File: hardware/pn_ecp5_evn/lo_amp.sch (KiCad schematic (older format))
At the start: 22 parts, among them J401 Conn_Coaxial, U301 PAT1220-C-3DB, U302 TRF37A73, U303 PAT1220-C-3DB

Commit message: first pass footprint assignment on pn r0
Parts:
- C301, C302, C303, C304, C305, C307, C308: footprint (none) -> Capacitor_SMD:C_0402_1005Metric
- C306, C309: footprint (none) -> Capacitor_SMD:C_0603_1608Metric
- J401: footprint (none) -> Connector_Coaxial:U.FL_Hirose_U.FL-R-SMT-1_Vertical
- L301, L302, L303: footprint (none) -> Inductor_SMD:L_0402_1005Metric
- R301, R302, R303, R304, R305, R306: footprint (none) -> Resistor_SMD:R_0402_1005Metric
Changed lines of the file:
@@
 $Descr A4 11693 8268
 encoding utf-8
-Sheet 3 9
+Sheet 4 9
 Title ""
 Date ""
@@
 F 0 "R401" H 3659 4396 50  0000 L CNN
 F 1 "50" H 3659 4305 50  0000 L CNN
-F 2 "" H 3600 4350 50  0001 C CNN
+F 2 "Resistor_SMD:R_0402_1005Metric" H 3600 4350 50  0001 C CNN
 F 3 "~" H 3600 4350 50  0001 C CNN
 	1    3600 4350
@@
 F 0 "C402" V 3950 4100 50  0000 C CNN
 F 1 "10 nF" V 3950 4350 50  0000 C CNN
-F 2 "" H 4000 4200 50  0001 C CNN
+F 2 "Capacitor_SMD:C_0402_1005Metric" H 4000 4200 50  0001 C CNN
 F 3 "~" H 4000 4200 50  0001 C CNN
 	1    4000 4200
@@
 F 0 "C403" V 3950 4800 50  0000 C CNN
 F 1 "10 nF" V 3950 5050 50  0000 C CNN
-F 2 "" H 4000 4900 50  0001 C CNN
+F 2 "Capacitor_SMD:C_0402_1005Metric" H 4000 4900 50  0001 C CNN
 F 3 "~" H 4000 4900 50  0001 C CNN
 	1    4000 4900
@@
 F 0 "R402" H 3659 4796 50  0000 L CNN
 F 1 "50" H 3659 4705 50  0000 L CNN
-F 2 "" H 3600 4750 50  0001 C CNN
+F 2 "Resistor_SMD:R_0402_1005Metric" H 3600 4750 50  0001 C CNN
 F 3 "~" H 3600 4750 50  0001 C CNN
 	1    3600 4750
@@
 F 0 "C401" V 3300 4500 50  0000 C CNN
 F 1 "10 nF" V 3500 4600 50  0000 C CNN
-F 2 "" H 3400 4550 50  0001 C CNN
+F 2 "Capacitor_SMD:C_0402_1005Metric" H 3400 4550 50  0001 C CNN
 F 3 "~" H 3400 4550 50  0001 C CNN
 	1    3400 4550
@@
 F 0 "L401" V 3950 4550 50  0000 C CNN
 F 1 "18 nH" V 3800 4500 50  0000 C CNN
-F 2 "" H 3850 4550 50  0001 C CNN
+F 2 "Inductor_SMD:L_0402_1005Metric" H 3850 4550 50  0001 C CNN
 F 3 "~" H 3850 4550 50  0001 C CNN
 	1    3850 4550
@@
 F 0 "R404" H 4459 4946 50  0000 L CNN
 F 1 "50" H 4459 4855 50  0000 L CNN
-F 2 "" H 4400 4900 50  0001 C CNN
+F 2 "Resistor_SMD:R_0402_1005Metric" H 4400 4900 50  0001 C CNN
 F 3 "~" H 4400 4900 50  0001 C CNN
 	1    4400 4900
@@
 F 0 "C404" V 5321 4200 50  0000 C CNN
 F 1 "10 nF" V 5412 4200 50  0000 C CNN
-F 2 "" H 5550 4200 50  0001 C CNN
+F 2 "Capacitor_SMD:C_0402_1005Metric" H 5550 4200 50  0001 C CNN
 F 3 "~" H 5550 4200 50  0001 C CNN
 	1    5550 4200
@@
 F 0 "C407" V 6571 4200 50  0000 C CNN
 F 1 "10 nF" V 6662 4200 50  0000 C CNN
-F 2 "" H 6800 4200 50  0001 C CNN
+F 2 "Capacitor_SMD:C_0402_1005Metric" H 6800 4200 50  0001 C CNN
 F 3 "~" H 6800 4200 50  0001 C CNN
 	1    6800 4200
@@
 F 0 "L403" H 6498 3646 50  0000 L CNN
 F 1 "BLM15GG471" H 6498 3555 50  0000 L CNN
-F 2 "" H 6450 3600 50  0001 C CNN
+F 2 "Inductor_SMD:L_0402_1005Metric" H 6450 3600 50  0001 C CNN
 F 3 "~" H 6450 3600 50  0001 C CNN
 	1    6450 3600
@@
 F 0 "C405" H 5742 3146 50  0000 L CNN
 F 1 "100 nF" H 5742 3055 50  0000 L CNN
-F 2 "" H 5650 3100 50  0001 C CNN
+F 2 "Capacitor_SMD:C_0402_1005Metric" H 5650 3100 50  0001 C CNN
 F 3 "~" H 5650 3100 50  0001 C CNN
 	1    5650 3100
@@
 F 0 "C409" H 7592 3146 50  0000 L CNN
 F 1 "10 uF" H 7592 3055 50  0000 L CNN
-F 2 "" H 7500 3100 50  0001 C CNN
+F 2 "Capacitor_SMD:C_0603_1608Metric" H 7500 3100 50  0001 C CNN
 F 3 "~" H 7500 3100 50  0001 C CNN
 	1    7500 3100
@@
 F 0 "C408" H 7192 3146 50  0000 L CNN
 F 1 "10 nF" H 7192 3055 50  0000 L CNN
-F 2 "" H 7100 3100 50  0001 C CNN
+F 2 "Capacitor_SMD:C_0402_1005Metric" H 7100 3100 50  0001 C CNN
 F 3 "~" H 7100 3100 50  0001 C CNN
 	1    7100 3100
@@
 F 0 "C406" H 6742 3146 50  0000 L CNN
 F 1 "390 pF" H 6742 3055 50  0000 L CNN
-F 2 "" H 6650 3100 50  0001 C CNN
+F 2 "Capacitor_SMD:C_0603_1608Metric" H 6650 3100 50  0001 C CNN
 F 3 "~" H 6650 3100 50  0001 C CNN
 	1    6650 3100
@@
 F 0 "J401" H 4900 5175 50  0000 L CNN
 F 1 "Conn_Coaxial" H 4900 5084 50  0000 L CNN
-F 2 "" H 4800 5200 50  0001 C CNN
+F 2 "Connector_Coaxial:U.FL_Hirose_U.FL-R-SMT-1_Vertical" H 4800 5200 50  0001 C CNN
 F 3 " ~" H 4800 5200 50  0001 C CNN
 	1    4800 5200
@@
 F 0 "R405" H 4459 5246 50  0000 L CNN
 F 1 "DNI" H 4459 5155 50  0000 L CNN
-F 2 "" H 4400 5200 50  0001 C CNN
+F 2 "Resistor_SMD:R_0402_1005Metric" H 4400 5200 50  0001 C CNN
 F 3 "~" H 4400 5200 50  0001 C CNN
 	1    4400 5200
@@
 F 0 "L402" H 6498 2446 50  0000 L CNN
 F 1 "BLM15GG471" H 6498 2355 50  0000 L CNN
-F 2 "" H 6450 2400 50  0001 C CNN
+F 2 "Inductor_SMD:L_0402_1005Metric" H 6450 2400 50  0001 C CNN
 F 3 "~" H 6450 2400 50  0001 C CNN
 	1    6450 2400
@@
 F 0 "R403" H 4459 3946 50  0000 L CNN
 F 1 "DNI" H 4459 3855 50  0000 L CNN
-F 2 "" H 4400 3900 50  0001 C CNN
+F 2 "Resistor_SMD:R_0402_1005Metric" H 4400 3900 50  0001 C CNN
 F 3 "~" H 4400 3900 50  0001 C CNN
 	1    4400 3900
@@
 F 0 "R406" H 6009 3746 50  0000 L CNN
 F 1 "DNI" H 6009 3655 50  0000 L CNN
-F 2 "" H 5950 3700 50  0001 C CNN
+F 2 "Resistor_SMD:R_0402_1005Metric" H 5950 3700 50  0001 C CNN
 F 3 "~" H 5950 3700 50  0001 C CNN
 	1    5950 3700

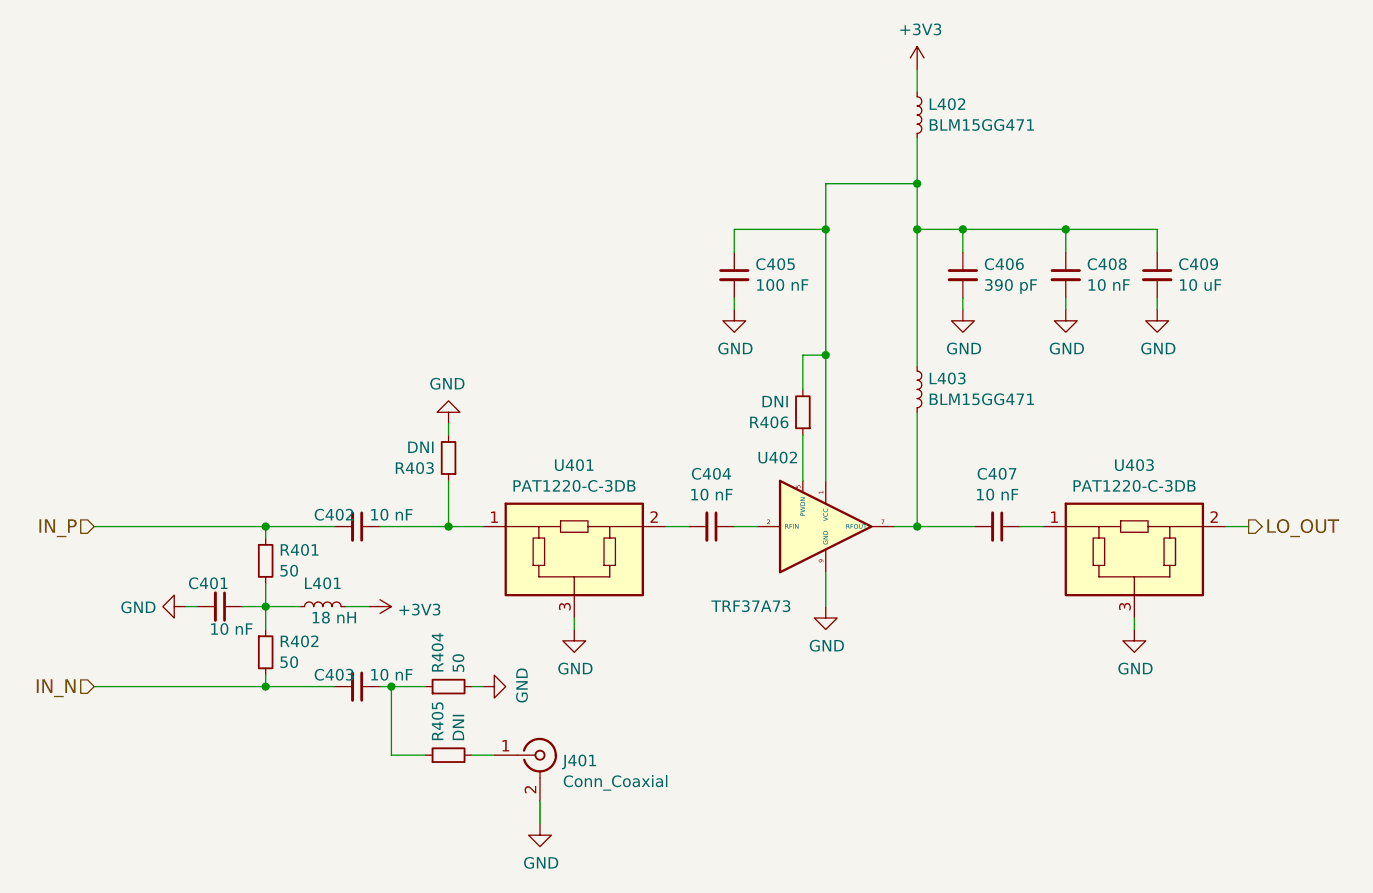
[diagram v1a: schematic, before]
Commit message: layout of phase noise downconverter
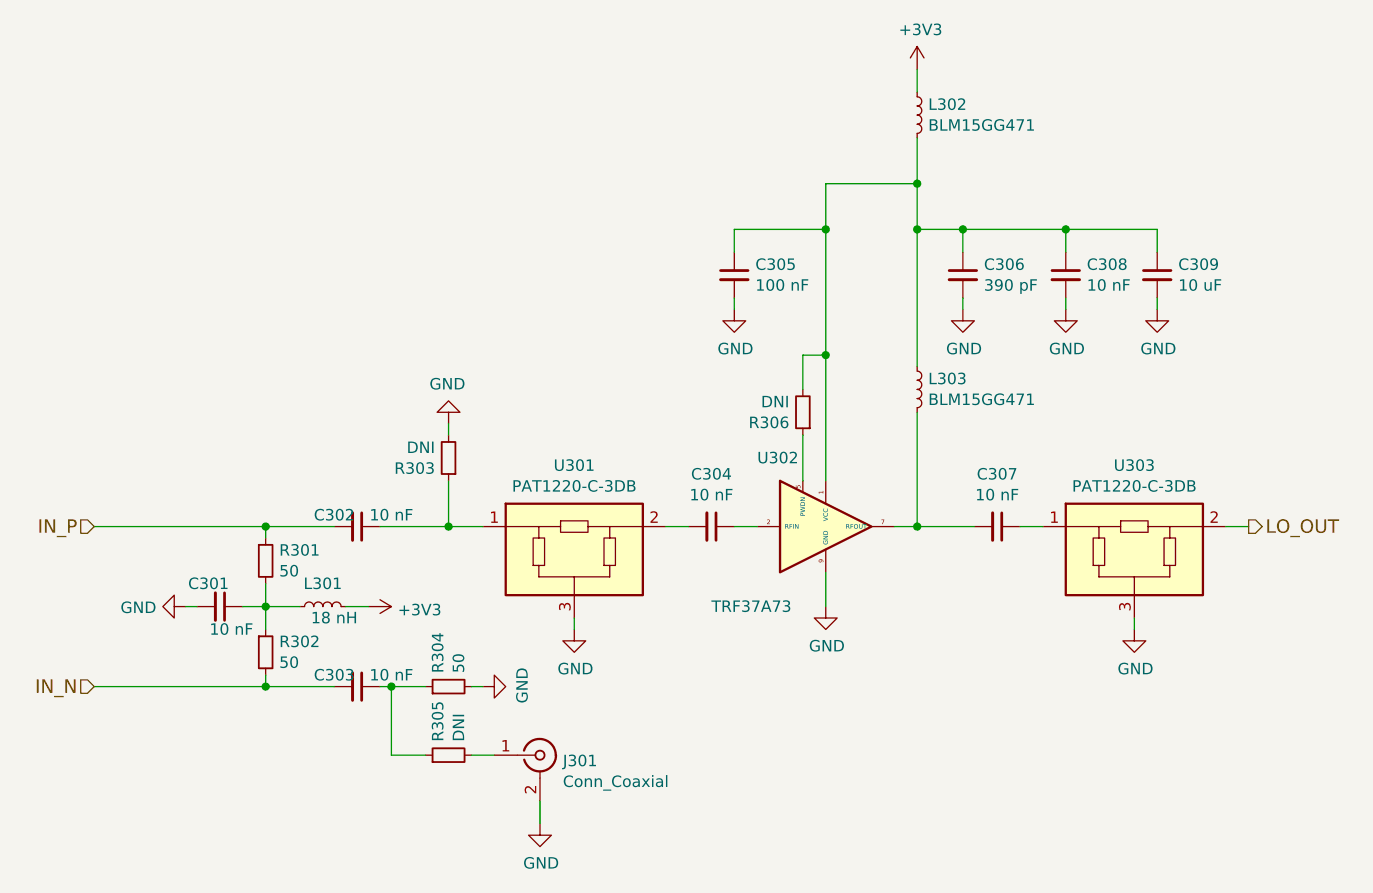
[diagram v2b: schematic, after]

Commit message: layout of phase noise downconverter
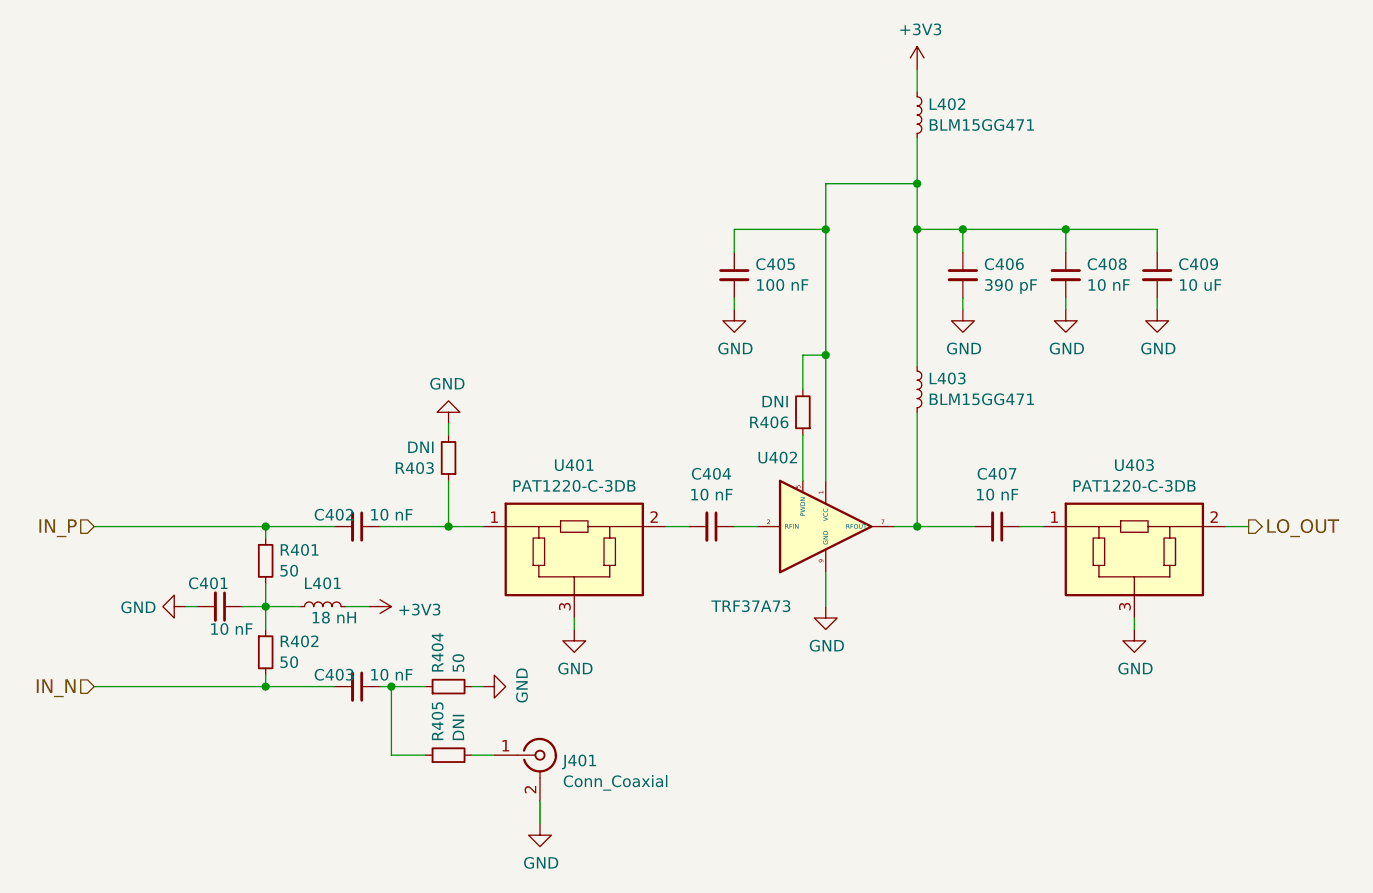
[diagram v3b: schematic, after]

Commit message: added part numbers to schematic of phase noise downconverter, ordered
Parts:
- C301, C302, C303, C304, C305, C307, C308, C309, J401, R303, R305, R306: Distributor Part Number (none) -> N/A
- C306: Distributor Part Number (none) -> 399-1069-1-ND
- L301: Distributor (none) -> Digi-Key; Distributor Part Number (none) -> 490-1172-1-ND
- L302, L303: Distributor (none) -> Digi-Key; Distributor Part Number (none) -> 490-5198-1-ND
- R301, R302, R304: Distributor (none) -> Digi-Key; Distributor Part Number (none) -> RR05R49.9DCT-ND
- U301, U303: Distributor (none) -> Digi-Key; Distributor Part Number (none) -> PAT123CT-ND
- U302: Distributor (none) -> Digi-Key; Distributor Part Number (none) -> 296-48786-1-ND
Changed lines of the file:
@@
 F 2 "Resistor_SMD:R_0402_1005Metric" H 3600 4350 50  0001 C CNN
 F 3 "~" H 3600 4350 50  0001 C CNN
+F 4 "Digi-Key" H 3600 4350 50  0001 C CNN "Distributor"
+F 5 "RR05R49.9DCT-ND" H 3600 4350 50  0001 C CNN "Distributor Part Number"
 	1    3600 4350
 	1    0    0    -1
@@
 F 2 "Package_SON:WSON-8-1EP_2x2mm_P0.5mm_EP0.9x1.6mm" H 6150 4200 50  0001 C CNN
 F 3 "http://www.ti.com/lit/ds/symlink/trf37a73.pdf" H 5950 4200 50  0001 C CNN
+F 4 "Digi-Key" H 5950 4200 50  0001 C CNN "Distributor"
+F 5 "296-48786-1-ND " H 5950 4200 50  0001 C CNN "Distributor Part Number"
 	1    5950 4200
 	1    0    0    -1
@@
 F 2 "Capacitor_SMD:C_0402_1005Metric" H 4000 4200 50  0001 C CNN
 F 3 "~" H 4000 4200 50  0001 C CNN
+F 4 "N/A" H 4000 4200 50  0001 C CNN "Distributor Part Number"
 	1    4000 4200
 	0    1    1    0
@@
 F 2 "Capacitor_SMD:C_0402_1005Metric" H 4000 4900 50  0001 C CNN
 F 3 "~" H 4000 4900 50  0001 C CNN
+F 4 "N/A" H 4000 4900 50  0001 C CNN "Distributor Part Number"
 	1    4000 4900
 	0    1    1    0
@@
 F 2 "Resistor_SMD:R_0402_1005Metric" H 3600 4750 50  0001 C CNN
 F 3 "~" H 3600 4750 50  0001 C CNN
+F 4 "Digi-Key" H 3600 4750 50  0001 C CNN "Distributor"
+F 5 "RR05R49.9DCT-ND" H 3600 4750 50  0001 C CNN "Distributor Part Number"
 	1    3600 4750
 	1    0    0    -1
@@
 F 2 "Capacitor_SMD:C_0402_1005Metric" H 3400 4550 50  0001 C CNN
 F 3 "~" H 3400 4550 50  0001 C CNN
+F 4 "N/A" H 3400 4550 50  0001 C CNN "Distributor Part Number"
 	1    3400 4550
 	0    1    1    0
@@
 F 2 "Inductor_SMD:L_0402_1005Metric" H 3850 4550 50  0001 C CNN
 F 3 "~" H 3850 4550 50  0001 C CNN
+F 4 "Digi-Key" H 3850 4550 50  0001 C CNN "Distributor"
+F 5 "490-1172-1-ND " H 3850 4550 50  0001 C CNN "Distributor Part Number"
 	1    3850 4550
 	0    -1   -1   0
@@
 F 2 "Resistor_SMD:R_0402_1005Metric" H 4400 4900 50  0001 C CNN
 F 3 "~" H 4400 4900 50  0001 C CNN
+F 4 "Digi-Key" H 4400 4900 50  0001 C CNN "Distributor"
+F 5 "RR05R49.9DCT-ND" H 4400 4900 50  0001 C CNN "Distributor Part Number"
 	1    4400 4900
 	0    -1   -1   0
@@
 F 2 "RF_Converter:RF_Attenuator_Susumu_PAT1220" H 4950 4300 50  0001 C CNN
 F 3 "https://www.susumu.co.jp/common/pdf/n_catalog_partition16_en.pdf" H 4700 4550 50  0001 C CNN
+F 4 "Digi-Key" H 4950 4300 50  0001 C CNN "Distributor"
+F 5 "PAT123CT-ND " H 4950 4300 50  0001 C CNN "Distributor Part Number"
 	1    4950 4300
 	1    0    0    -1
@@
 F 2 "Capacitor_SMD:C_0402_1005Metric" H 5550 4200 50  0001 C CNN
 F 3 "~" H 5550 4200 50  0001 C CNN
+F 4 "N/A" H 5550 4200 50  0001 C CNN "Distributor Part Number"
 	1    5550 4200
 	0    1    1    0
@@
 F 2 "Capacitor_SMD:C_0402_1005Metric" H 6800 4200 50  0001 C CNN
 F 3 "~" H 6800 4200 50  0001 C CNN
+F 4 "N/A" H 6800 4200 50  0001 C CNN "Distributor Part Number"
 	1    6800 4200
 	0    1    1    0
@@
 F 2 "RF_Converter:RF_Attenuator_Susumu_PAT1220" H 7400 4300 50  0001 C CNN
 F 3 "https://www.susumu.co.jp/common/pdf/n_catalog_partition16_en.pdf" H 7150 4550 50  0001 C CNN
+F 4 "Digi-Key" H 7400 4300 50  0001 C CNN "Distributor"
+F 5 "PAT123CT-ND " H 7400 4300 50  0001 C CNN "Distributor Part Number"
 	1    7400 4300
 	1    0    0    -1
@@
 F 2 "Inductor_SMD:L_0402_1005Metric" H 6450 3600 50  0001 C CNN
 F 3 "~" H 6450 3600 50  0001 C CNN
+F 4 "Digi-Key" H 6450 3600 50  0001 C CNN "Distributor"
+F 5 "490-5198-1-ND" H 6450 3600 50  0001 C CNN "Distributor Part Number"
 	1    6450 3600
 	1    0    0    -1
@@
 F 2 "Capacitor_SMD:C_0402_1005Metric" H 5650 3100 50  0001 C CNN
 F 3 "~" H 5650 3100 50  0001 C CNN
+F 4 "N/A" H 5650 3100 50  0001 C CNN "Distributor Part Number"
 	1    5650 3100
 	1    0    0    -1
@@
 F 2 "Capacitor_SMD:C_0603_1608Metric" H 7500 3100 50  0001 C CNN
 F 3 "~" H 7500 3100 50  0001 C CNN
+F 4 "N/A" H 7500 3100 50  0001 C CNN "Distributor Part Number"
 	1    7500 3100
 	1    0    0    -1
@@
 F 2 "Capacitor_SMD:C_0402_1005Metric" H 7100 3100 50  0001 C CNN
 F 3 "~" H 7100 3100 50  0001 C CNN
+F 4 "N/A" H 7100 3100 50  0001 C CNN "Distributor Part Number"
 	1    7100 3100
 	1    0    0    -1
@@
 F 2 "Capacitor_SMD:C_0603_1608Metric" H 6650 3100 50  0001 C CNN
 F 3 "~" H 6650 3100 50  0001 C CNN
+F 4 "399-1069-1-ND" H 6650 3100 50  0001 C CNN "Distributor Part Number"
 	1    6650 3100
 	1    0    0    -1
@@
 F 2 "Connector_Coaxial:U.FL_Hirose_U.FL-R-SMT-1_Vertical" H 4800 5200 50  0001 C CNN
 F 3 " ~" H 4800 5200 50  0001 C CNN
+F 4 "N/A" H 4800 5200 50  0001 C CNN "Distributor Part Number"
 	1    4800 5200
 	1    0    0    -1
@@
 F 2 "Resistor_SMD:R_0402_1005Metric" H 4400 5200 50  0001 C CNN
 F 3 "~" H 4400 5200 50  0001 C CNN
+F 4 "N/A" H 4400 5200 50  0001 C CNN "Distributor Part Number"
 	1    4400 5200
 	0    -1   -1   0
@@
 F 2 "Inductor_SMD:L_0402_1005Metric" H 6450 2400 50  0001 C CNN
 F 3 "~" H 6450 2400 50  0001 C CNN
+F 4 "Digi-Key" H 6450 2400 50  0001 C CNN "Distributor"
+F 5 "490-5198-1-ND" H 6450 2400 50  0001 C CNN "Distributor Part Number"
 	1    6450 2400
 	1    0    0    -1
@@
 F 2 "Resistor_SMD:R_0402_1005Metric" H 4400 3900 50  0001 C CNN
 F 3 "~" H 4400 3900 50  0001 C CNN
+F 4 "N/A" H 4400 3900 50  0001 C CNN "Distributor Part Number"
 	1    4400 3900
 	-1   0    0    1
@@
 F 2 "Resistor_SMD:R_0402_1005Metric" H 5950 3700 50  0001 C CNN
 F 3 "~" H 5950 3700 50  0001 C CNN
+F 4 "N/A" H 5950 3700 50  0001 C CNN "Distributor Part Number"
 	1    5950 3700
 	-1   0    0    1
